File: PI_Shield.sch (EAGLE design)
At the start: 64 parts, among them Q1 220mA/50V/3.5Ω, Q3 220mA/50V/3.5Ω, Q4 220mA/50V/3.5Ω, Q5 2.5A/30V/105mΩ, U1 MAX1136EUA-T, U2 AZ1117EH-3.3TRG1, Y1 ECS-80-S-4X

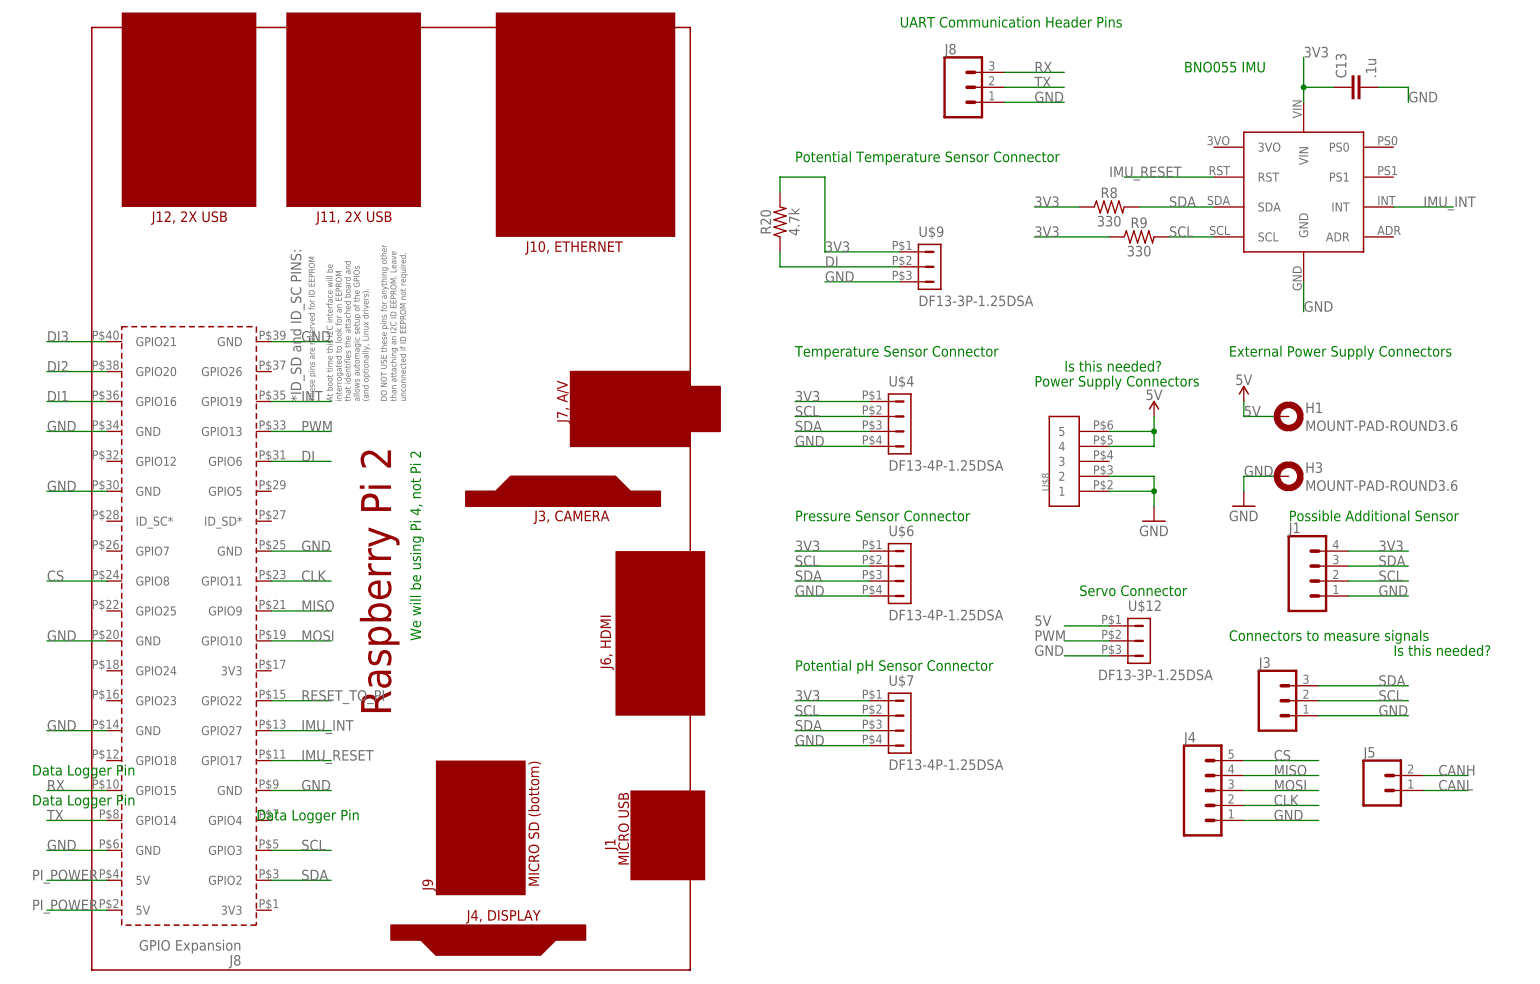
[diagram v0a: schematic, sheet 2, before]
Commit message: Fixes for the GND
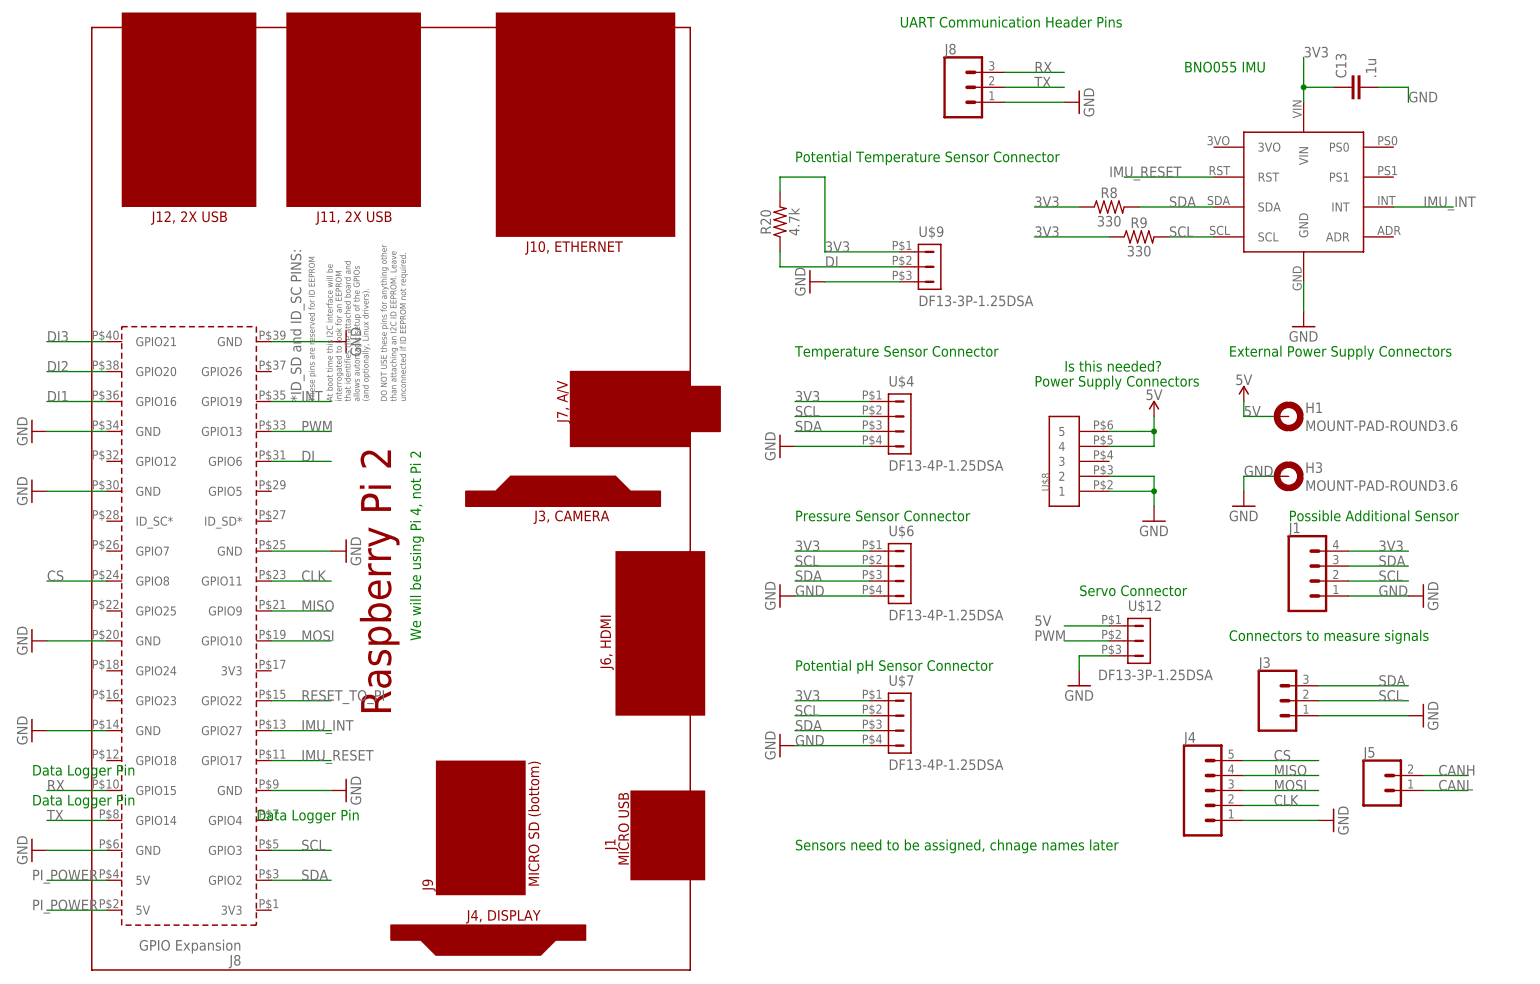
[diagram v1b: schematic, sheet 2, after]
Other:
- note added: "Sensors need to be assigned, chnage names later"

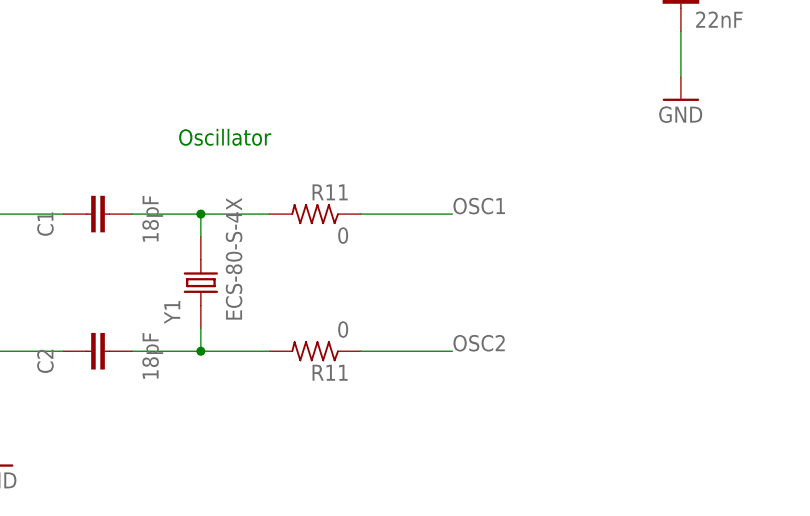
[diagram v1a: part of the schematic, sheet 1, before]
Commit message: fixed some errors
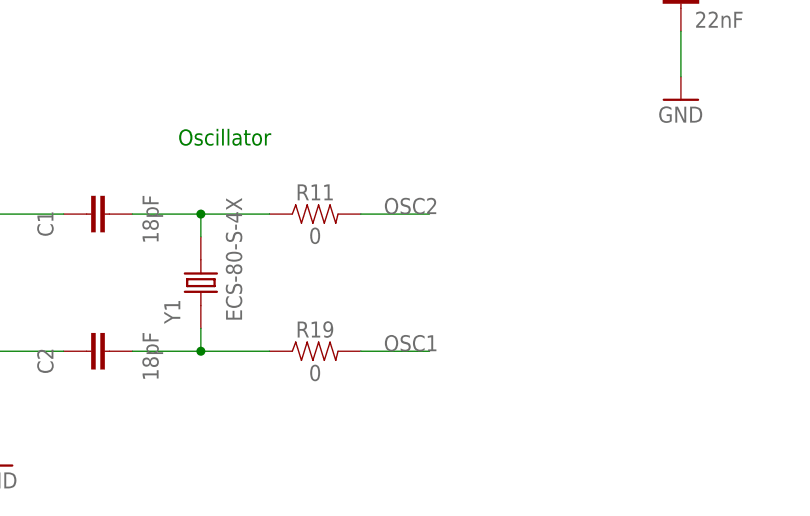
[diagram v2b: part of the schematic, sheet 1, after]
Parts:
- removed 0: R11, Resistor_Capacitor:RC0603JR-070RL
- added R19: 0, SparkFun-Resistors:RESISTOR0603
- R11: device Resistor_Capacitor:RC0603JR-070RL -> SparkFun-Resistors:RESISTOR0603
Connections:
- removed net N$4: 0.1
- removed net N$5: R11.1
- net N$2: now also R11.1; no longer 0.2
- net N$3: now also R19.1; no longer R11.2
- net OSC1: now also R19.2
- net OSC2: now also R11.2
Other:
- moved on the sheet: R11
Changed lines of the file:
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@@
 <part name="C1" library="Resistor_Capacitor" library_urn="urn:adsk.eagle:library:11396451" deviceset="C0603C180J5GACTU" device="" package3d_urn="urn:adsk.eagle:package:10872909/3" value="18pF"/>
 <part name="C2" library="Resistor_Capacitor" library_urn="urn:adsk.eagle:library:11396451" deviceset="C0603C180J5GACTU" device="" package3d_urn="urn:adsk.eagle:package:10872909/3" value="18pF"/>
-<part name="0" library="Resistor_Capacitor" library_urn="urn:adsk.eagle:library:11396451" deviceset="RC0603JR-070RL" device="" package3d_urn="urn:adsk.eagle:package:10872900/2" value="R11"/>
-<part name="R11" library="Resistor_Capacitor" library_urn="urn:adsk.eagle:library:11396451" deviceset="RC0603JR-070RL" device="" package3d_urn="urn:adsk.eagle:package:10872900/2" value="0"/>
 <part name="Y1" library="ECS-80-S-4X" deviceset="ECS-80-S-4X" device=""/>
 <part name="GND1" library="supply1" library_urn="urn:adsk.eagle:library:371" deviceset="GND" device=""/>
@@
 <part name="GND38" library="supply1" library_urn="urn:adsk.eagle:library:371" deviceset="GND" device=""/>
 <part name="GND39" library="supply1" library_urn="urn:adsk.eagle:library:371" deviceset="GND" device=""/>
+<part name="R11" library="SparkFun-Resistors" library_urn="urn:adsk.eagle:library:532" deviceset="RESISTOR" device="0603" package3d_urn="urn:adsk.eagle:package:39650/1" value="0"/>
+<part name="R19" library="SparkFun-Resistors" library_urn="urn:adsk.eagle:library:532" deviceset="RESISTOR" device="0603" package3d_urn="urn:adsk.eagle:package:39650/1" value="0"/>
 </parts>
 <sheets>
@@
 <attribute name="VALUE" x="38.481" y="32.258" size="1.778" layer="96" rot="R90"/>
 </instance>
-<instance part="0" gate="G$1" x="55.88" y="50.8" smashed="yes" rot="R180">
-<attribute name="NAME" x="59.69" y="49.3014" size="1.778" layer="95" rot="R180"/>
-<attribute name="VALUE" x="59.69" y="54.102" size="1.778" layer="96" rot="R180"/>
-</instance>
-<instance part="R11" gate="G$1" x="55.88" y="35.56" smashed="yes" rot="R180">
-<attribute name="NAME" x="59.69" y="34.0614" size="1.778" layer="95" rot="R180"/>
-<attribute name="VALUE" x="59.69" y="38.862" size="1.778" layer="96" rot="R180"/>
-</instance>
 <instance part="Y1" gate="G$1" x="43.18" y="43.18" smashed="yes" rot="R90">
 <attribute name="NAME" x="40.891540625" y="38.60306875" size="1.77991875" layer="95" rot="R90"/>
@@
 <instance part="GND11" gate="1" x="236.22" y="43.18" smashed="yes" rot="R90">
 <attribute name="VALUE" x="238.76" y="40.64" size="1.778" layer="96" rot="R90"/>
+</instance>
+<instance part="R11" gate="G$1" x="55.88" y="50.8" smashed="yes">
+<attribute name="NAME" x="55.88" y="52.324" size="1.778" layer="95" font="vector" align="bottom-center"/>
+<attribute name="VALUE" x="55.88" y="49.276" size="1.778" layer="96" font="vector" align="top-center"/>
+</instance>
+<instance part="R19" gate="G$1" x="55.88" y="35.56" smashed="yes">
+<attribute name="NAME" x="55.88" y="37.084" size="1.778" layer="95" font="vector" align="bottom-center"/>
+<attribute name="VALUE" x="55.88" y="34.036" size="1.778" layer="96" font="vector" align="top-center"/>
 </instance>
 </instances>
@@
 <segment>
 <pinref part="C1" gate="G$1" pin="2"/>
-<pinref part="0" gate="G$1" pin="2"/>
 <wire x1="35.56" y1="50.8" x2="43.18" y2="50.8" width="0.1524" layer="91"/>
 <pinref part="Y1" gate="G$1" pin="2"/>
@@
 <wire x1="43.18" y1="48.26" x2="43.18" y2="50.8" width="0.1524" layer="91"/>
 <junction x="43.18" y="50.8"/>
+<pinref part="R11" gate="G$1" pin="1"/>
 </segment>
 </net>
 <net name="N$3" class="0">
 <segment>
-<pinref part="R11" gate="G$1" pin="2"/>
 <pinref part="C2" gate="G$1" pin="2"/>
 <wire x1="50.8" y1="35.56" x2="43.18" y2="35.56" width="0.1524" layer="91"/>
@@
 <wire x1="43.18" y1="38.1" x2="43.18" y2="35.56" width="0.1524" layer="91"/>
 <junction x="43.18" y="35.56"/>
-</segment>
-</net>
-<net name="N$4" class="0">
-<segment>
-<pinref part="0" gate="G$1" pin="1"/>
-<wire x1="60.96" y1="50.8" x2="71.12" y2="50.8" width="0.1524" layer="91"/>
-</segment>
-</net>
-<net name="N$5" class="0">
-<segment>
-<pinref part="R11" gate="G$1" pin="1"/>
-<wire x1="60.96" y1="35.56" x2="71.12" y2="35.56" width="0.1524" layer="91"/>
+<pinref part="R19" gate="G$1" pin="1"/>
 </segment>
 </net>
@@
 <wire x1="30.48" y1="127" x2="17.78" y2="127" width="0.1524" layer="91"/>
 <label x="17.78" y="127" size="1.778" layer="95"/>
-<label x="71.12" y="50.8" size="1.778" layer="95"/>
+</segment>
+<segment>
+<pinref part="R19" gate="G$1" pin="2"/>
+<wire x1="60.96" y1="35.56" x2="68.58" y2="35.56" width="0.1524" layer="91"/>
+<label x="63.5" y="35.56" size="1.778" layer="95"/>
 </segment>
 </net>
@@
 <wire x1="30.48" y1="129.54" x2="17.78" y2="129.54" width="0.1524" layer="91"/>
 <label x="17.78" y="129.54" size="1.778" layer="95"/>
-<label x="71.12" y="35.56" size="1.778" layer="95"/>
-</segment>
-</net>
+</segment>
+<segment>
+<pinref part="R11" gate="G$1" pin="2"/>
+<wire x1="60.96" y1="50.8" x2="68.58" y2="50.8" width="0.1524" layer="91"/>
+<label x="63.5" y="50.8" size="1.778" layer="95"/>
+</segment>
+</net>
